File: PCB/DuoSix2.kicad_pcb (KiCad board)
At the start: 2 copper layers, 92 x 58 mm, 38 parts, among them J1 OLED_DISPLAY, SW1 SW_Push_45deg, SW2 SW_Push_45deg, SW3 SW_Push_45deg, SW4 SW_Push_45deg, SW5 SW_Push_45deg, SW6 SW_Push_45deg, SW7 RotaryEncoder_Switch, SW8 RotaryEncoder_Switch, U1 MOUDLE-SEEEDUINO-XIAO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

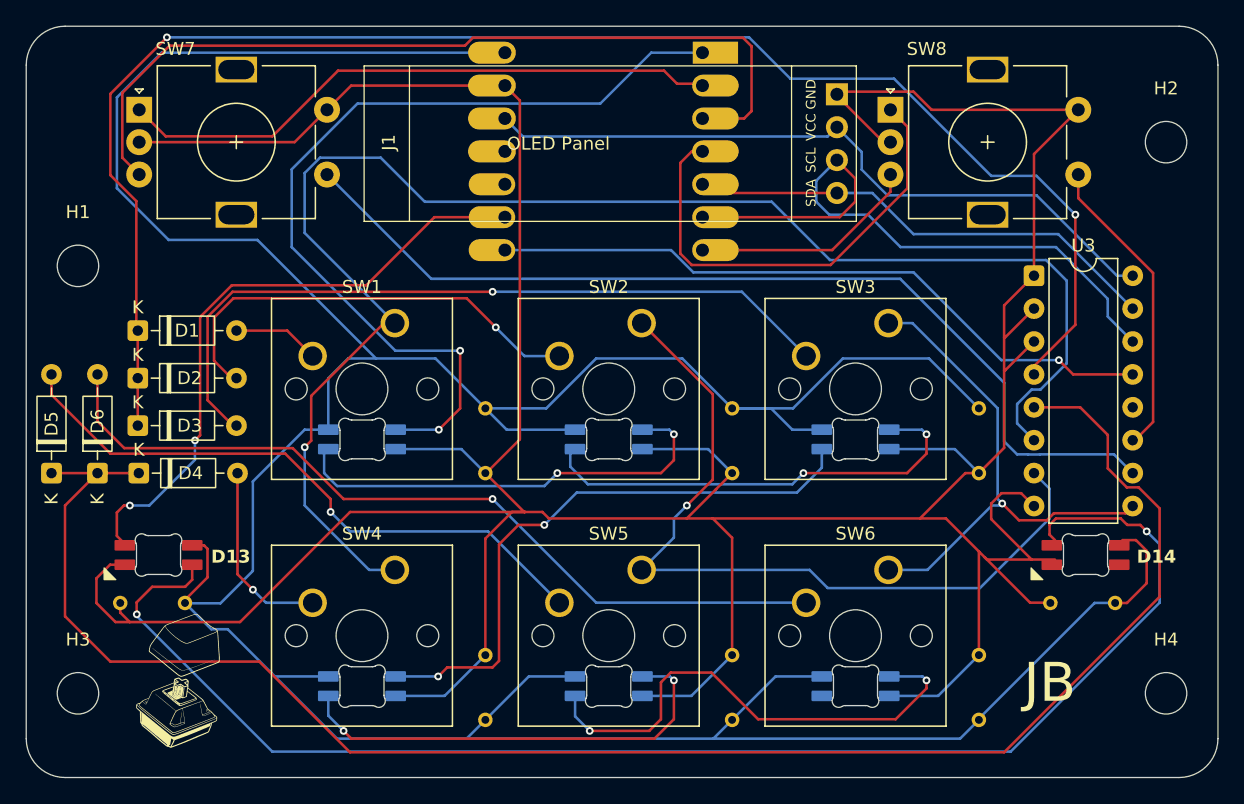
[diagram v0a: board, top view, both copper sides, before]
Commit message: Altered Design
Removed decoupling capacitors and IC socket to reduce production cost
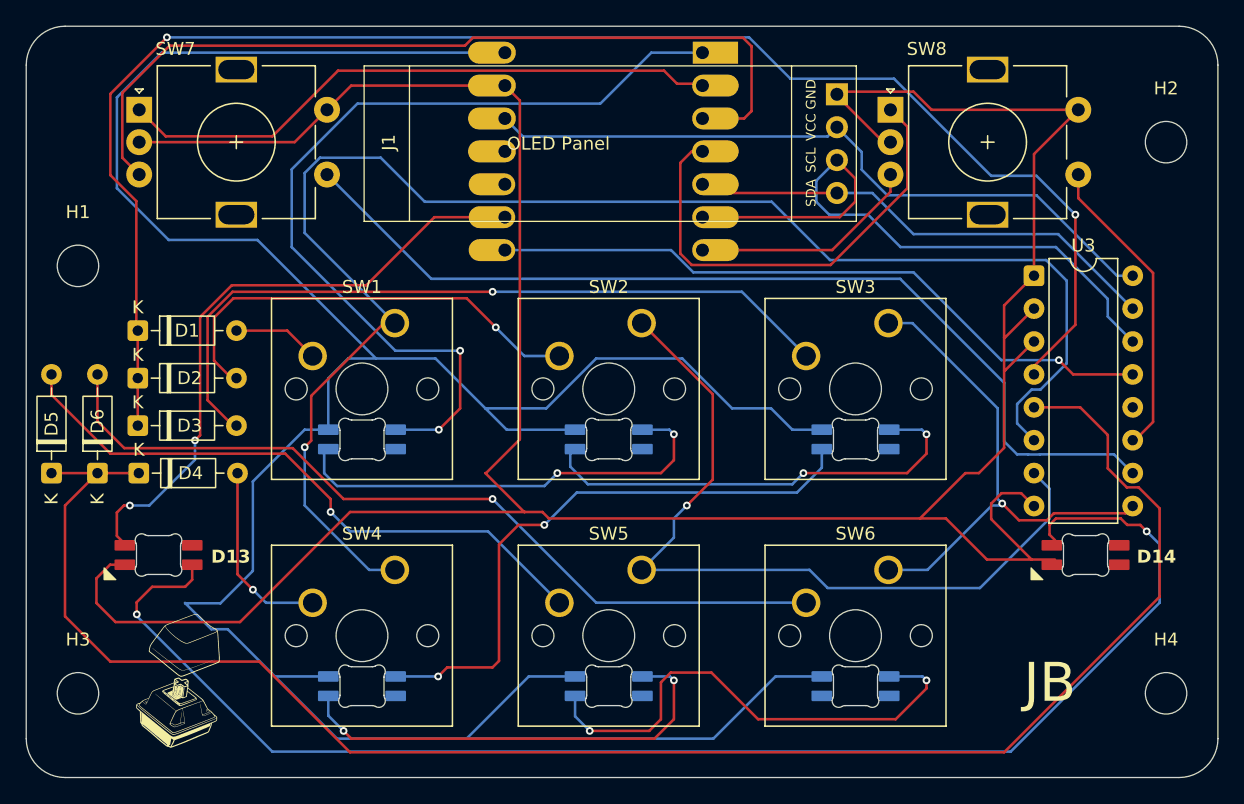
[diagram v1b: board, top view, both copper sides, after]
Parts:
- removed C1, C2, C3, C4, C5, C6, C7, C8: 0.1 μF, 0.1 uF Ceramic Capacitor Through Hole:CAP_Z5UH6UJ5R_VIS
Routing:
- net GND: track 321.9 -> 228.4 mm
- net +5V: track 282.0 -> 210.3 mm

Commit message: Updated PCB
Forgot some traces after changing model in last version
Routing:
- net GND: track 228.4 -> 334.5 mm, vias 0 -> 8
- net +5V: track 210.3 -> 254.4 mm, vias 0 -> 2
